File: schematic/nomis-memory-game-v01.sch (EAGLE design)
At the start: 3 parts, among them J1 AVR_SPI_PRG_6NS

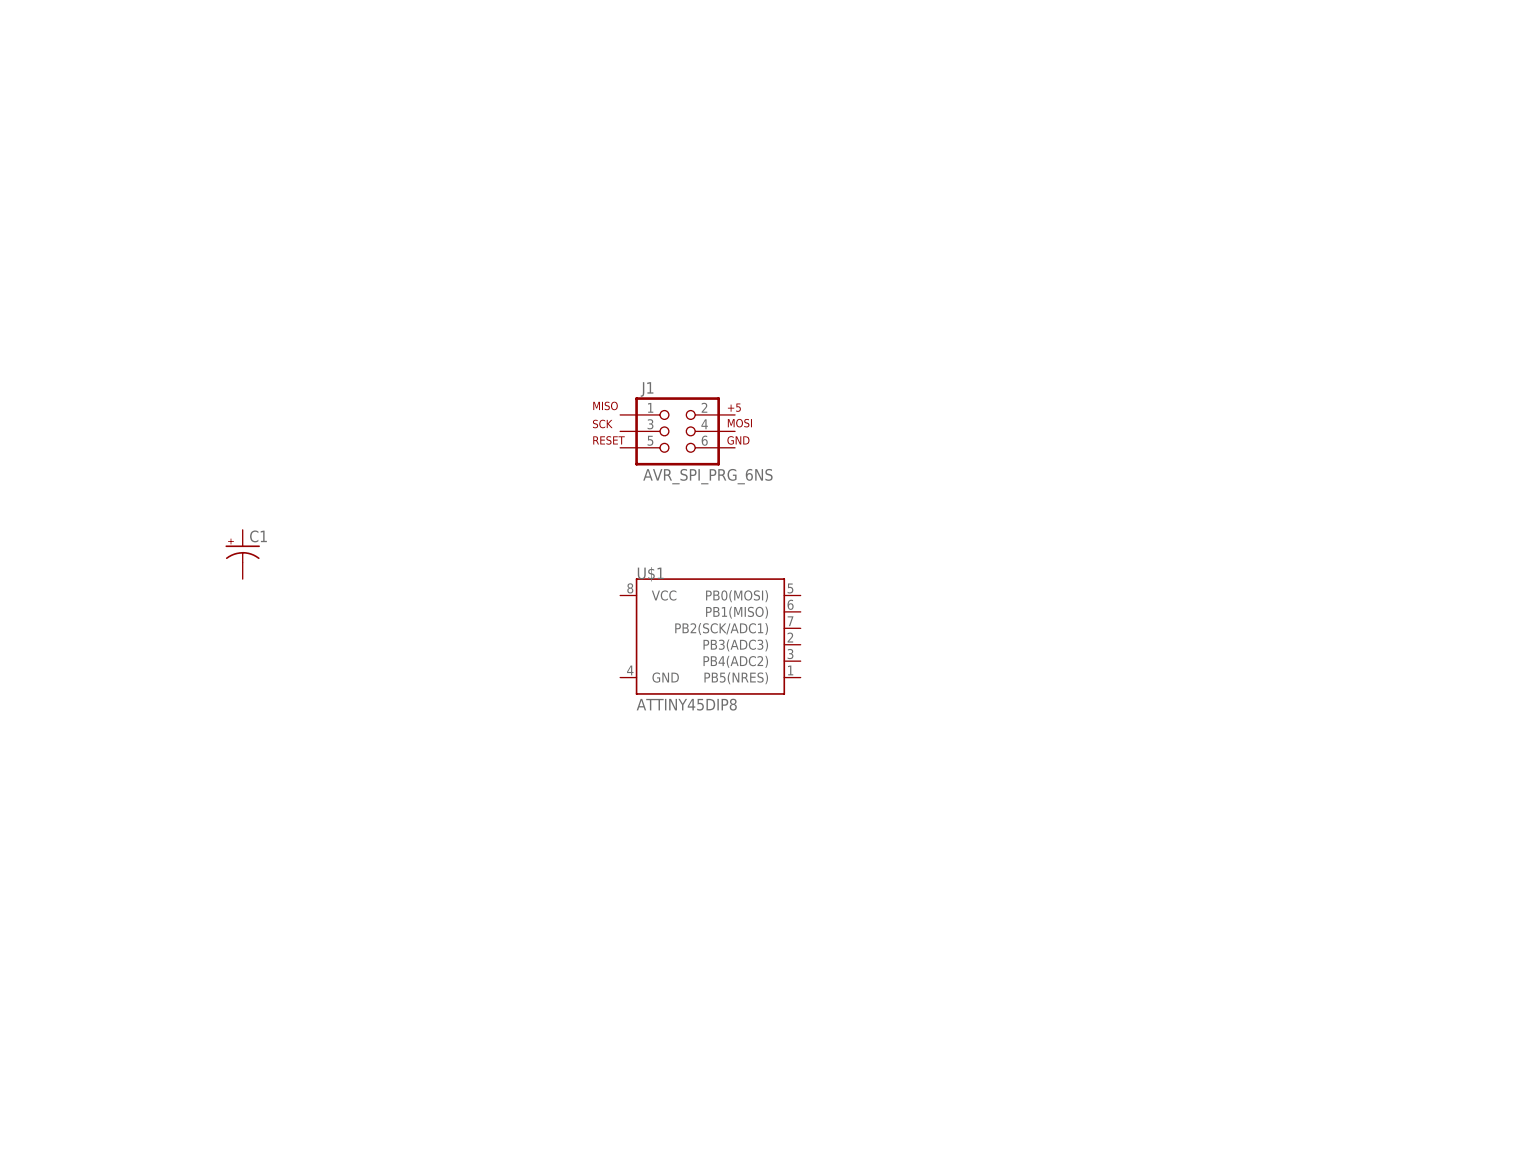
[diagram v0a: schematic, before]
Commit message: Added Schematic File
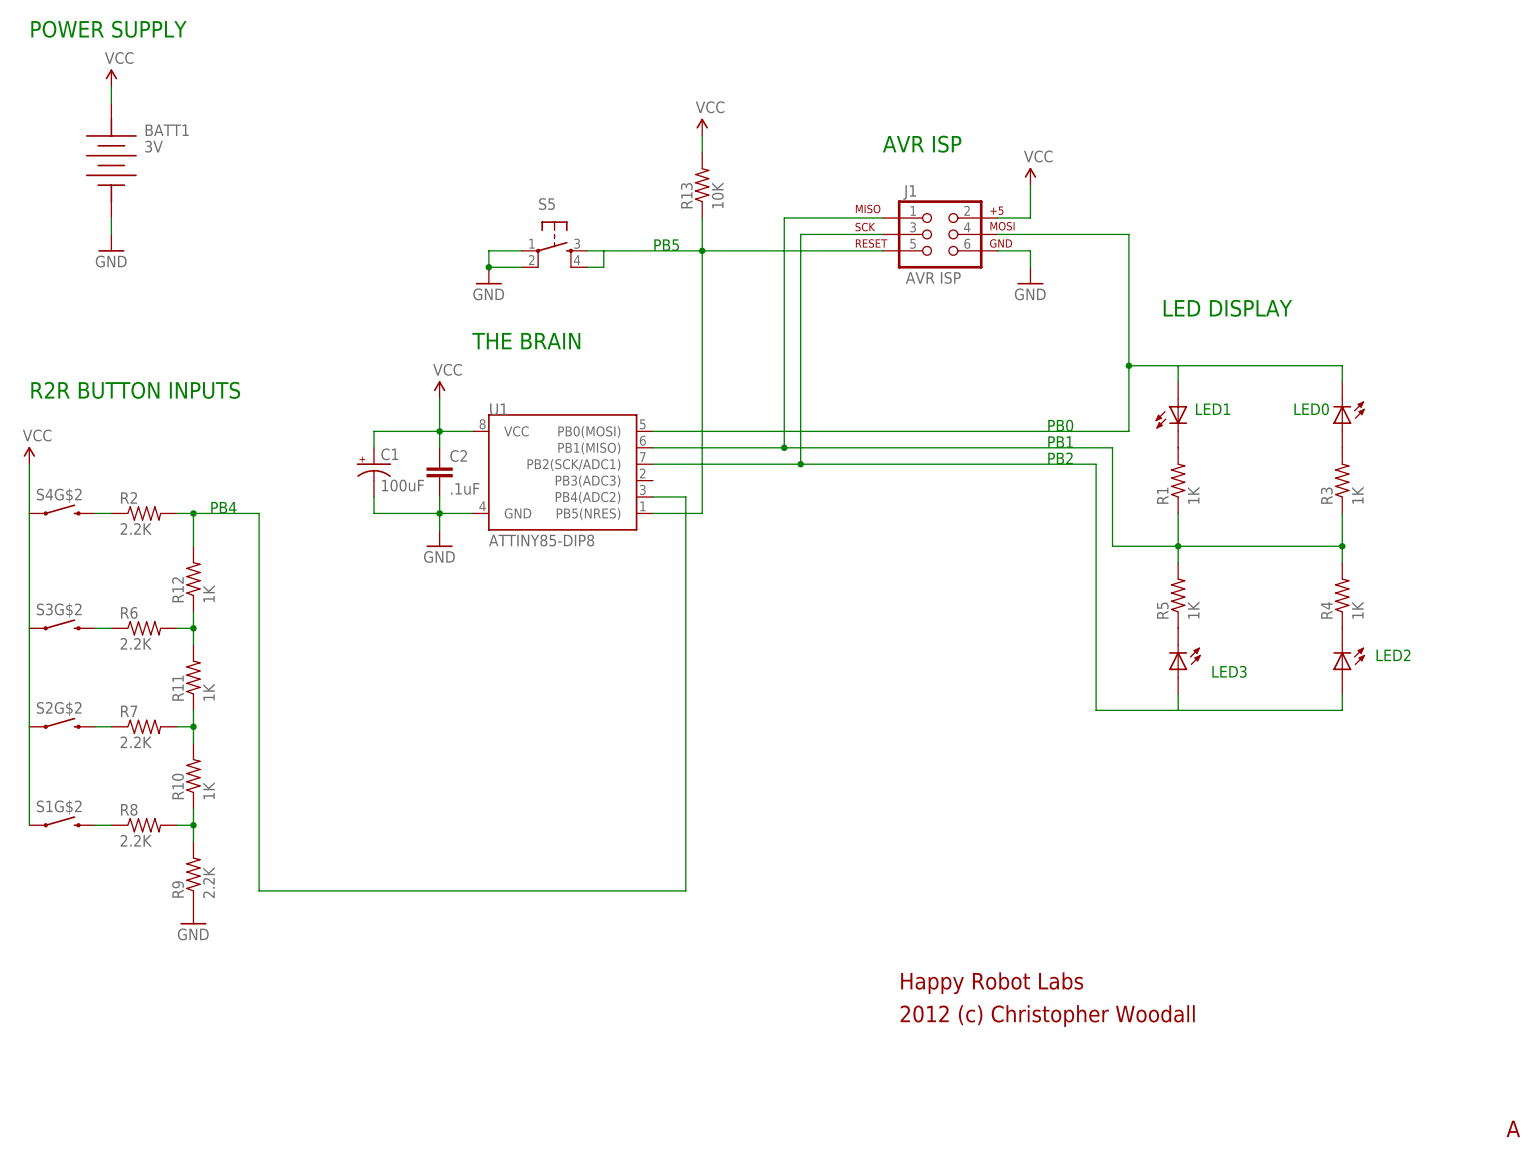
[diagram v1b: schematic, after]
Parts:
- removed U$1: ATTINY45DIP8, SparkFun:ATTINY45DIP8
- added BATT1: 3V, SparkFun:FKIT-COIN_CELLLIR2450-H
- added C2: .1uF, SparkFun:CAPPTH
- added R1, R10, R11, R12, R3, R4, R5: 1K, SparkFun:RESISTORPTH-1/4W
- added R13: 10K, SparkFun:RESISTORPTH-1/4W
- added R2, R6, R7, R8, R9: 2.2K, SparkFun:RESISTORPTH-1/4W
- added S1, S2, S3, S4: SWITCH-MOMENTARY-LED-SPLIT, nomis-memory-game:SWITCH-MOMENTARY-LED-SPLIT
- added S5: (no value), SparkFun:TAC_SWITCHPTH
- added U1: ATTINY85-DIP8, SparkFun:ATTINY45DIP8
- C1: value (none) -> 100uF
- J1: value AVR_SPI_PRG_6NS -> AVR ISP
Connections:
- new net GND: BATT1.NEG, C1.-, C2.2, J1.6, R9.1, S5.1, S5.2, U1.GND
- new net N$1: R3.2, S1G$1.A
- new net N$10: J1.5, R13.1, S5.3, S5.4, U1.PB5(NRES)
- new net N$11: R12.2, R2.2, U1.PB4(ADC2)
- new net N$12: R2.1, S4G$2.2
- new net N$13: R6.1, S3G$2.2
- new net N$14: R7.1, S2G$2.2
- new net N$15: R8.1, S1G$2.2
- new net N$16: R11.2, R12.1, R6.2
- new net N$2: R1.2, S2G$1.C
- new net N$3: R4.1, S3G$1.C
- new net N$4: R5.1, S4G$1.C
- new net N$5: J1.1, R1.1, R3.1, R4.2, R5.2, U1.PB1(MISO)
- new net N$6: J1.3, S3G$1.A, S4G$1.A, U1.PB2(SCK/ADC1)
- new net N$7: J1.4, S1G$1.C, S2G$1.A, U1.PB0(MOSI)
- new net N$8: R10.1, R8.2, R9.2
- new net N$9: R10.2, R11.1, R7.2
- new net VCC: BATT1.POS, C1.+, C2.1, J1.2, R13.2, S1G$2.1, S2G$2.1, S3G$2.1, S4G$2.1, U1.VCC
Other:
- note added: "2012 (c) Christopher Woodall"
- note added: "A"
- note added: "AVR ISP"
- note added: "Happy Robot Labs"
- note added: "LED DISPLAY"
- note added: "LED0"
- note added: "LED1"
- note added: "LED2"
- note added: "LED3"
- note added: "PB0"
- note added: "PB1"
- note added: "PB2"
- note added: "PB4"
- note added: "PB5"
- note added: "POWER SUPPLY"
- note added: "R2R BUTTON INPUTS"
- note added: "THE BRAIN"
- moved on the sheet: C1, J1

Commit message: Added PCB board layout and edited the schematic a bit to fit the PCB board. Need to clean up a few things yet
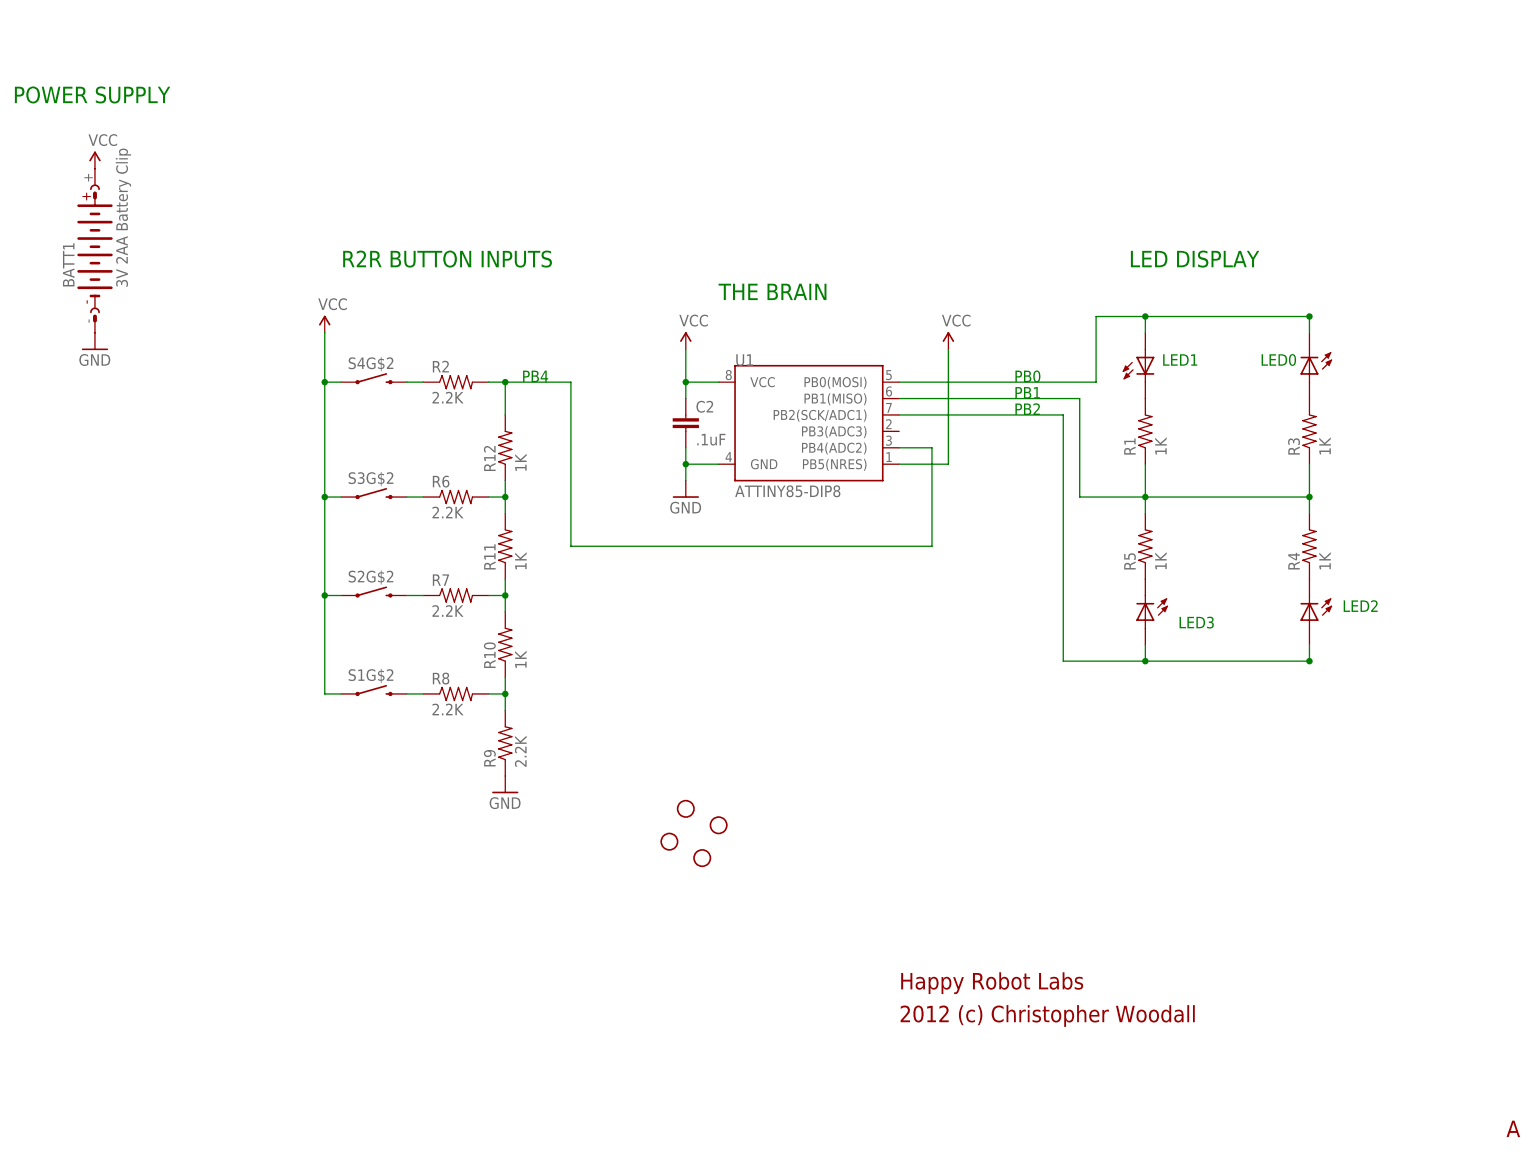
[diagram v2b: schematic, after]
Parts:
- removed C1: 100uF, SparkFun:CAP_POL1206
- removed J1: AVR ISP, SparkFun:AVR_SPI_PRG_6NS
- removed R13: 10K, SparkFun:RESISTORPTH-1/4W
- removed S5: (no value), SparkFun:TAC_SWITCHPTH
- added JP1, JP2, JP3, JP4: STAND-OFFTIGHT, SparkFun:STAND-OFFTIGHT
- BATT1: value 3V -> 3V 2AA Battery Clip; device SparkFun:FKIT-COIN_CELLLIR2450-H -> battery:AB9V
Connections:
- removed net N$10: J1.5, R13.1, S5.3, S5.4, U1.PB5(NRES)
- net GND: now also BATT1.-; no longer BATT1.NEG, C1.-, J1.6, S5.1, S5.2
- net N$5: no longer J1.1
- net N$6: no longer J1.3
- net N$7: no longer J1.4
- net VCC: now also BATT1.+, U1.PB5(NRES); no longer BATT1.POS, C1.+, J1.2, R13.2
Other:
- note removed: "AVR ISP"
- note removed: "PB5"
- moved on the sheet: C2, R1, R10, R11, R12, R2, R3, R4, R5, R6, R7, R8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
